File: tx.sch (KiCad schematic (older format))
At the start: 37 parts, among them T2 Transformer_1P_SS, U10 TLV2464CD, U11 SN74CBT3253

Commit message: Added RF front end and LNA
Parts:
- added C? (x6): 100n, Capacitor_SMD:C_0603_1608Metric, symbol DeltaSDR-rescue:C-Device-DeltaSDR-rescue
- added C? (x2): 5n6, Capacitor_SMD:C_0603_1608Metric, symbol DeltaSDR-rescue:C-Device-DeltaSDR-rescue
- added D?: BAP64-06, symbol Device:D_x2_ACom_KKA
- added L? (x3): 15u, symbol Device:L
- added L?: 390n, symbol Device:L
- added Q? (x2): BSS123, Package_TO_SOT_SMD:SOT-23, symbol Transistor_FET:BSS123
- added R? (x2): 2k2, Resistor_SMD:R_0603_1608Metric, symbol DeltaSDR-rescue:R-Device-DeltaSDR-rescue
- added R? (x2): 100k, Resistor_SMD:R_0603_1608Metric, symbol DeltaSDR-rescue:R-Device-DeltaSDR-rescue
- added R? (x2): 27R, Resistor_SMD:R_0603_1608Metric, symbol DeltaSDR-rescue:R-Device-DeltaSDR-rescue
- added R?: 270R, Resistor_SMD:R_0603_1608Metric, symbol DeltaSDR-rescue:R-Device-DeltaSDR-rescue
- added U?: MMG3H21NT1, Package_TO_SOT_SMD:SOT-89-3, symbol RF_Amplifier:SPF5189Z
- C34, C35, C36, C37, C38, C39, C40, C41, C42, C43, C44, C45, C46, C47, C48, C49, C50, C51: symbol DeltaSDR-rescue:C-Device -> DeltaSDR-rescue:C-Device-DeltaSDR-rescue
- R17, R18, R19, R20, R21, R22, R23, R24, R25, R26, R27, R28, R29, R30, R31, R32: symbol DeltaSDR-rescue:R-Device -> DeltaSDR-rescue:R-Device-DeltaSDR-rescue
- T2: symbol DeltaSDR-rescue:Transformer_1P_SS-Device -> DeltaSDR-rescue:Transformer_1P_SS-Device-DeltaSDR-rescue
- U10: symbol DeltaSDR-rescue:Opamp_Quad_Generic-Device -> DeltaSDR-rescue:Opamp_Quad_Generic-Device-DeltaSDR-rescue
- U11: symbol DeltaSDR-rescue:SN74CBT3253-Analog_Switch -> DeltaSDR-rescue:SN74CBT3253-Analog_Switch-DeltaSDR-rescue
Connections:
- net labels added: +12V, HI_RX, HI_TX, PA_IN, RX_RF
- wire segments 147 -> 203

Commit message: First layouting
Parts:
- removed C? (x6): 100n, Capacitor_SMD:C_0603_1608Metric, symbol DeltaSDR-rescue:C-Device-DeltaSDR-rescue
- removed C? (x2): 5n6, Capacitor_SMD:C_0603_1608Metric, symbol DeltaSDR-rescue:C-Device-DeltaSDR-rescue
- removed D?: BAP64-06, symbol Device:D_x2_ACom_KKA
- removed L? (x3): 15u, symbol Device:L
- removed L?: 390n, symbol Device:L
- removed Q? (x2): BSS123, Package_TO_SOT_SMD:SOT-23, symbol Transistor_FET:BSS123
- removed R? (x2): 2k2, Resistor_SMD:R_0603_1608Metric, symbol DeltaSDR-rescue:R-Device-DeltaSDR-rescue
- removed R? (x2): 100k, Resistor_SMD:R_0603_1608Metric, symbol DeltaSDR-rescue:R-Device-DeltaSDR-rescue
- removed R? (x2): 27R, Resistor_SMD:R_0603_1608Metric, symbol DeltaSDR-rescue:R-Device-DeltaSDR-rescue
- removed R?: 270R, Resistor_SMD:R_0603_1608Metric, symbol DeltaSDR-rescue:R-Device-DeltaSDR-rescue
- removed U?: MMG3H21NT1, Package_TO_SOT_SMD:SOT-89-3, symbol RF_Amplifier:SPF5189Z
- C43: footprint Capacitor_SMD:C_0603_1608Metric -> Capacitor_SMD:C_0805_2012Metric
- T2: footprint (none) -> Transformer_SMD:Transformer_MACOM_SM-22
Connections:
- net VOUTL-: no longer R24.1, R29.1, R32.1
- net at U11.10 (2B1), U11.3 (1B4): now also C49.1, R30.1; no longer C46.1, R26.1
- net at U11.11 (2B2), U11.4 (1B3): now also C40.1, R20.1; no longer C49.1, R30.1
- net at U11.12 (2B3), U11.5 (1B2): now also C46.1, R26.1; no longer C40.1, R20.1
- new net VOUTL+: R32.1
- new net VOUTR+: R24.1
- new net VOUTR-: R29.1

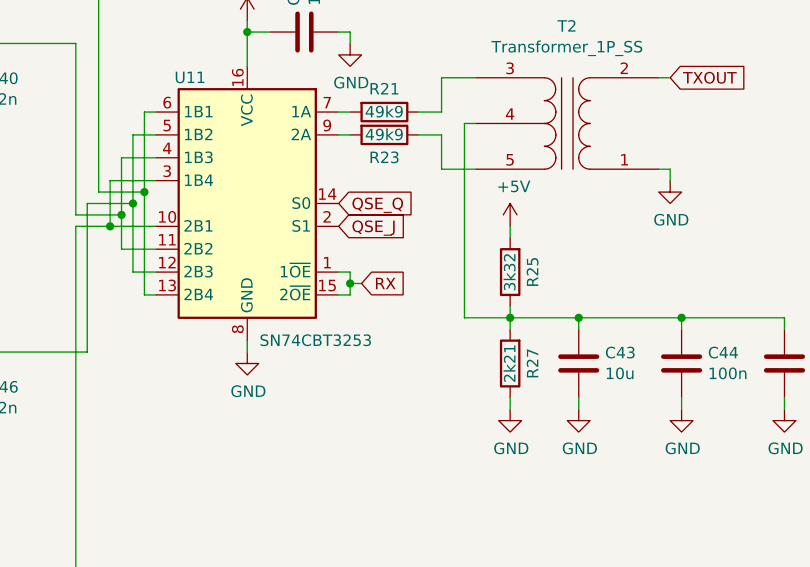
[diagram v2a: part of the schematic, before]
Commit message: Added remaining switching signals and polygons
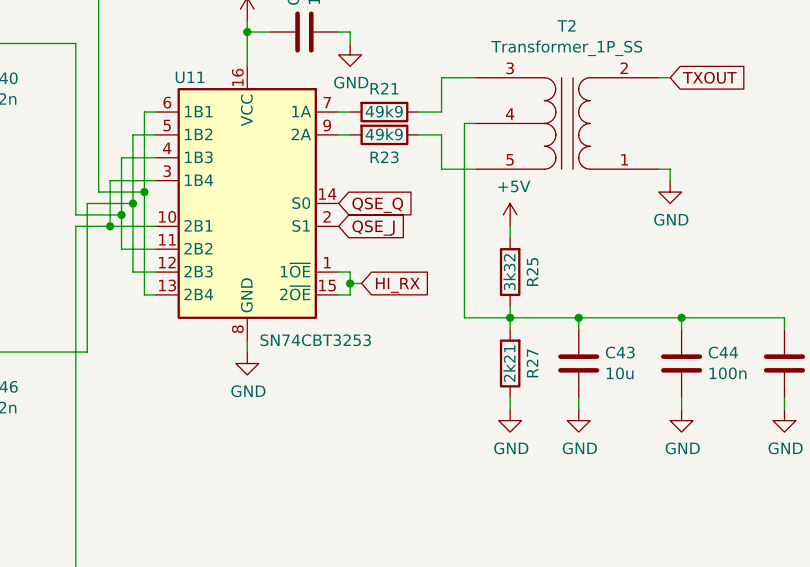
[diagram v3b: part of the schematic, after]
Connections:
- net RX renamed HI_RX
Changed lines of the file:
@@
 	4550 4050 4550 4100
 Text GLabel 4600 4050 2    50   Input ~ 0
-RX
+HI_RX
 $Comp
 L DeltaSDR-rescue:R-Device-DeltaSDR-rescue R?

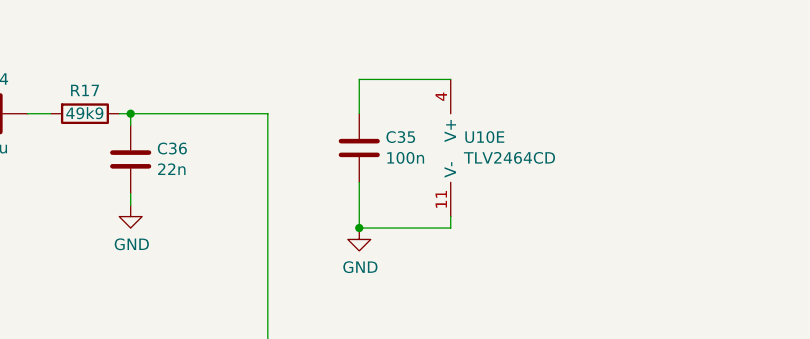
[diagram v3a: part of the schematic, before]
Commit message: ERC, DRC done, added output for ATU and AMP
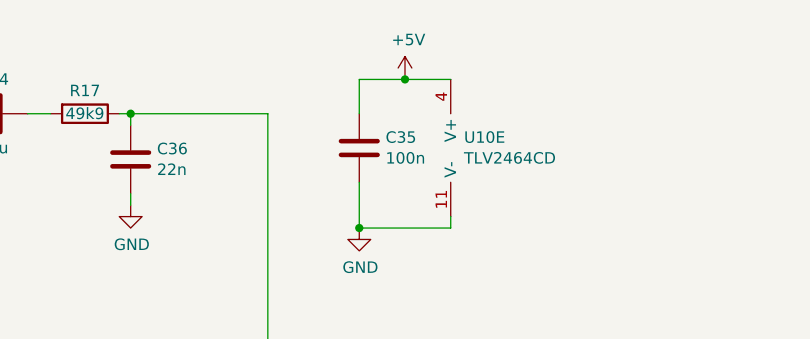
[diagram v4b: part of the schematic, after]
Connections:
- net +5V: now also C35.1, U10.4 (V+)
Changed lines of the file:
@@
 Connection ~ 3850 2100
 Wire Wire Line
-	4250 1450 3850 1450
+	4250 1450 4050 1450
 Wire Wire Line
 	3850 1450 3850 1600
@@
 	3350 3800 3350 5700
 Connection ~ 3500 3800
+$Comp
+L power:+5V #PWR?
+U 1 1 5EAA104E
+P 4050 1450
+AR Path="/5E9BB9DC/5EAA104E" Ref="#PWR?"  Part="1"
+AR Path="/5EAFBA6A/5EAA104E" Ref="#PWR0229"  Part="1"
+F 0 "#PWR0229" H 4050 1300 50  0001 C CNN
+F 1 "+5V" H 4065 1623 50  0000 C CNN
+F 2 "" H 4050 1450 50  0001 C CNN
+F 3 "" H 4050 1450 50  0001 C CNN
+	1    4050 1450
+	1    0    0    -1
+$EndComp
+Connection ~ 4050 1450
+Wire Wire Line
+	4050 1450 3850 1450
 $EndSCHEMATC

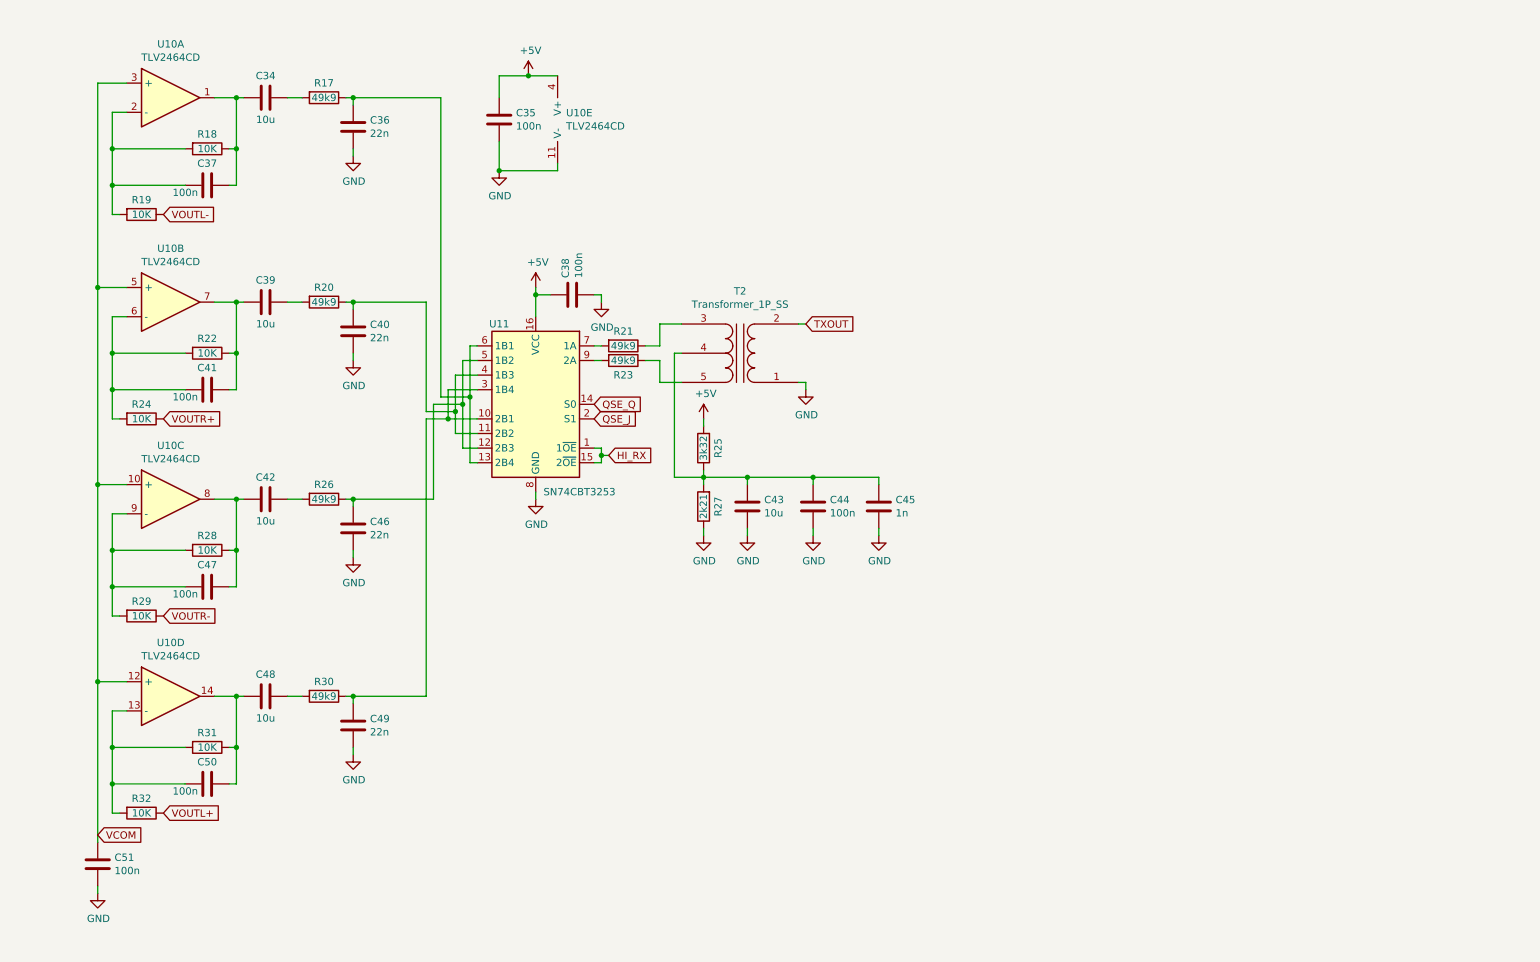
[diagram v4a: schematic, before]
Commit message: Corrected Q6 connection, RX schematic clean up
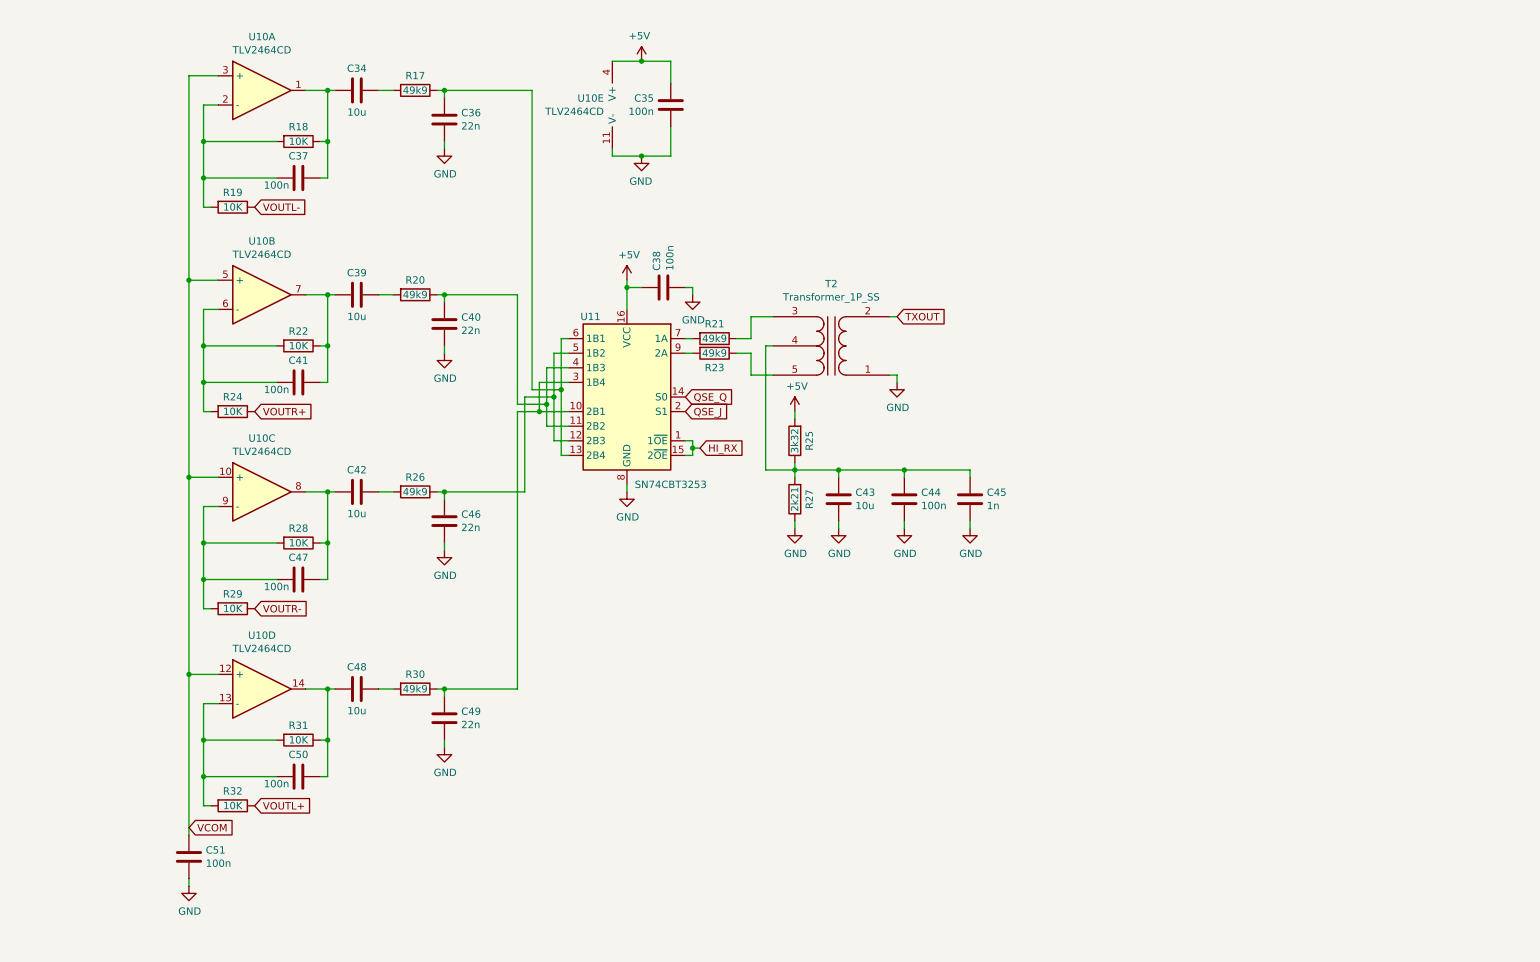
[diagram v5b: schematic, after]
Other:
- moved on the sheet: C34, C35, C36, C37, C38, C39, C40, C41, C42, C43, C44, C45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

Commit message: Changed mixers footprints, added 3D models, silk screen correction
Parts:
- U11: footprint Package_SO:SOIC-16_4.55x10.3mm_P1.27mm -> Package_SO:SOIC-16_3.9x9.9mm_P1.27mm
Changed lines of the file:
@@
 F 0 "U11" H 4975 4200 50  0000 C CNN
 F 1 "SN74CBT3253" H 4425 3050 50  0000 C CNN
-F 2 "Package_SO:SOIC-16_4.55x10.3mm_P1.27mm" H 4725 3650 50  0001 C CNN
+F 2 "Package_SO:SOIC-16_3.9x9.9mm_P1.27mm" H 4725 3650 50  0001 C CNN
 F 3 "http://www.ti.com/lit/gpn/sn74cbt3253" H 4725 3650 50  0001 C CNN
 	1    4725 3650

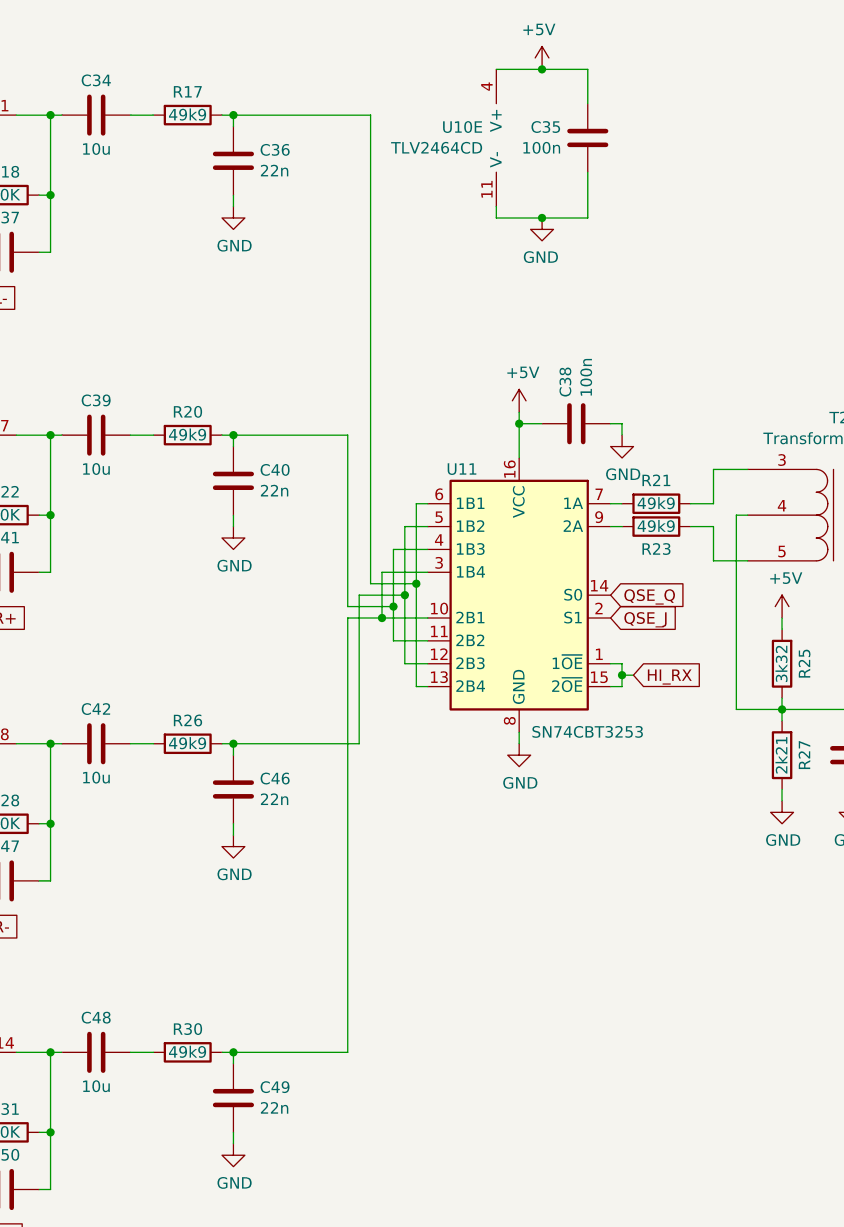
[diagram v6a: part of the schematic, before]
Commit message: Wrong TX resistors values correction.
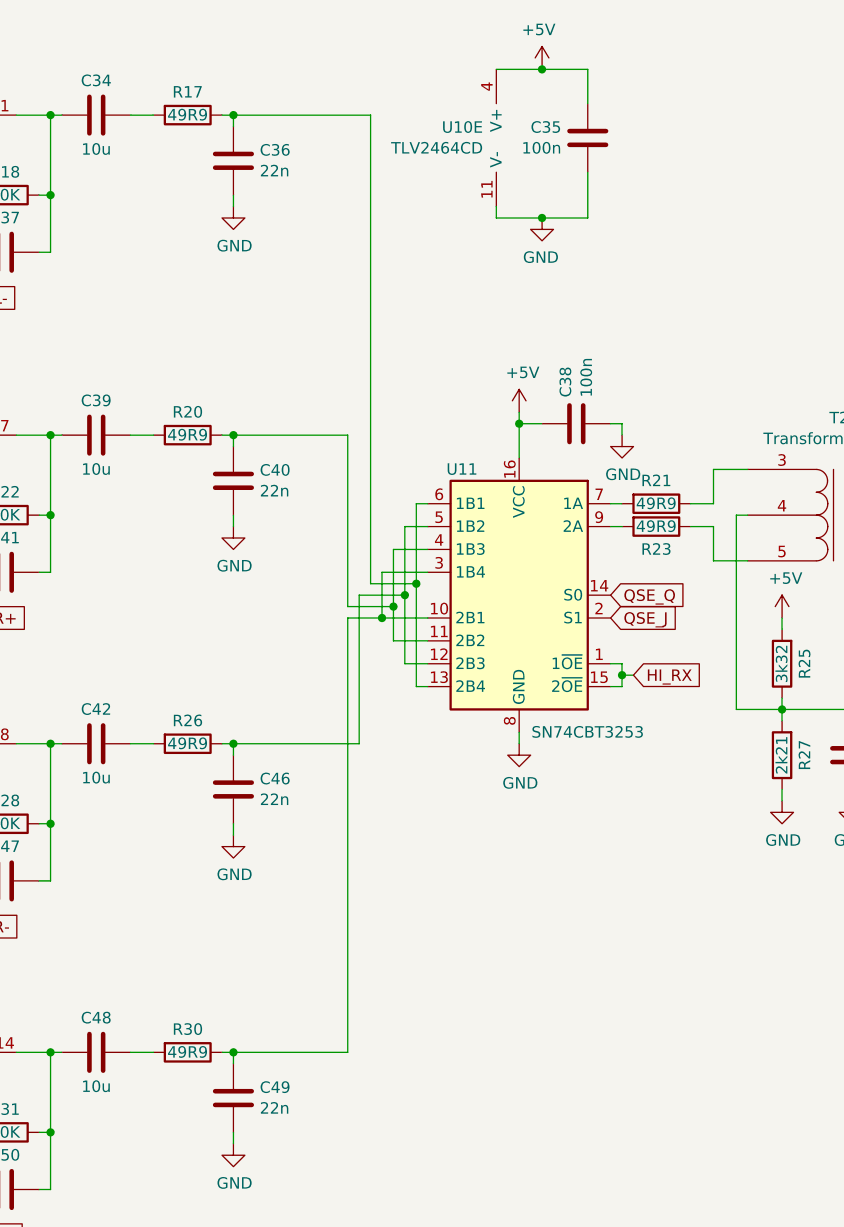
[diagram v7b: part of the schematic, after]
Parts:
- R17, R20, R21, R23, R26, R30: value 49k9 -> 49R9
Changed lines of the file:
@@
 AR Path="/5EAFBA6A/5EB0EF7D" Ref="R17"  Part="1"
 F 0 "R17" V 3175 1550 50  0000 C CNN
-F 1 "49k9" V 3275 1550 50  0000 C CNN
+F 1 "49R9" V 3275 1550 50  0000 C CNN
 F 2 "Resistor_SMD:R_0603_1608Metric" V 3205 1550 50  0001 C CNN
 F 3 "~" H 3275 1550 50  0001 C CNN
@@
 AR Path="/5EAFBA6A/5EB0EFBF" Ref="R20"  Part="1"
 F 0 "R20" V 3175 2950 50  0000 C CNN
-F 1 "49k9" V 3275 2950 50  0000 C CNN
+F 1 "49R9" V 3275 2950 50  0000 C CNN
 F 2 "Resistor_SMD:R_0603_1608Metric" V 3205 2950 50  0001 C CNN
 F 3 "~" H 3275 2950 50  0001 C CNN
@@
 AR Path="/5EAFBA6A/5EB0F001" Ref="R26"  Part="1"
 F 0 "R26" V 3175 4300 50  0000 C CNN
-F 1 "49k9" V 3275 4300 50  0000 C CNN
+F 1 "49R9" V 3275 4300 50  0000 C CNN
 F 2 "Resistor_SMD:R_0603_1608Metric" V 3205 4300 50  0001 C CNN
 F 3 "~" H 3275 4300 50  0001 C CNN
@@
 AR Path="/5EAFBA6A/5EB0F043" Ref="R30"  Part="1"
 F 0 "R30" V 3175 5650 50  0000 C CNN
-F 1 "49k9" V 3275 5650 50  0000 C CNN
+F 1 "49R9" V 3275 5650 50  0000 C CNN
 F 2 "Resistor_SMD:R_0603_1608Metric" V 3205 5650 50  0001 C CNN
 F 3 "~" H 3275 5650 50  0001 C CNN
@@
 AR Path="/5EAFBA6A/5EB0F0B3" Ref="R21"  Part="1"
 F 0 "R21" V 5225 3250 50  0000 C CNN
-F 1 "49k9" V 5325 3250 50  0000 C CNN
+F 1 "49R9" V 5325 3250 50  0000 C CNN
 F 2 "Resistor_SMD:R_0603_1608Metric" V 5255 3250 50  0001 C CNN
 F 3 "~" H 5325 3250 50  0001 C CNN
@@
 AR Path="/5EAFBA6A/5EB0F0B9" Ref="R23"  Part="1"
 F 0 "R23" V 5425 3350 50  0000 C CNN
-F 1 "49k9" V 5325 3350 50  0000 C CNN
+F 1 "49R9" V 5325 3350 50  0000 C CNN
 F 2 "Resistor_SMD:R_0603_1608Metric" V 5255 3350 50  0001 C CNN
 F 3 "~" H 5325 3350 50  0001 C CNN
